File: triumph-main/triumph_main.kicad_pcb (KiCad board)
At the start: 2 copper layers, 99.1 x 86.4 mm, 81 parts, among them J1 JST_XH_vert_01x04, J10 JST_XH_vert_01x04, J2 JST_PH_vert_01x03, J3 JST_PH_vert_01x03, J4 JST_PH_vert_01x06, J5 Conn_BNC, J6 JST_PH_vert_01x03, J7 JST_PH_vert_01x06, J8 JST_PH_vert_01x03, J9 JST_PH_vert_01x03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

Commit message: Add more labels
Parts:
- moved RV1 0.13 mm to (102.9, 83.7)
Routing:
- net GND: track 98.3 -> 93.4 mm
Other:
- board text added: "1"
- board text added: "2"
- board text added: "3"
- board text added: "4"
- board text added: "COM"
- board text added: "OUTPUT GAIN ADJ"
- board text added: "PRESCALE"
- board text added: "SINE"
- board text added: "SINE ADJ"
- board text added: "TRI GEN GAIN ADJ"
- board text removed: "SIN"
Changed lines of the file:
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@@
   (general
     (thickness 1.6)
-    (drawings 61)
+    (drawings 70)
     (tracks 415)
     (zones 0)
@@
     (descr "8-lead though-hole mounted DIP package, row spacing 7.62 mm (300 mils), Socket, LongPads")
     (tags "THT DIP DIL PDIP 2.54mm 7.62mm 300mil Socket LongPads")
-    (fp_text reference U3 (at 3.81 -2.33) (layer F.SilkS)
+    (fp_text reference U3 (at 3.81 10.16) (layer F.SilkS)
       (effects (font (size 1 1) (thickness 0.15)))
     )
@@
     (descr "Potentiometer, vertical, Bourns 3296W, https://www.bourns.com/pdfs/3296.pdf")
     (tags "Potentiometer vertical Bourns 3296W")
-    (fp_text reference RV5 (at -8.89 0 180) (layer F.SilkS)
+    (fp_text reference RV5 (at 3.556 -1.27 180) (layer F.SilkS)
       (effects (font (size 1 1) (thickness 0.15)))
     )
@@
     (descr "Potentiometer, vertical, Bourns 3296W, https://www.bourns.com/pdfs/3296.pdf")
     (tags "Potentiometer vertical Bourns 3296W")
-    (fp_text reference RV4 (at -2.54 -3.66 90) (layer F.SilkS)
+    (fp_text reference RV4 (at -6.604 -4.572 180) (layer F.SilkS)
       (effects (font (size 1 1) (thickness 0.15)))
     )
@@
     (descr "Potentiometer, vertical, Bourns 3296W, https://www.bourns.com/pdfs/3296.pdf")
     (tags "Potentiometer vertical Bourns 3296W")
-    (fp_text reference RV3 (at -2.54 -3.66 90) (layer F.SilkS)
+    (fp_text reference RV3 (at -6.604 4.572) (layer F.SilkS)
       (effects (font (size 1 1) (thickness 0.15)))
     )
@@
     (descr "Potentiometer, vertical, Bourns 3296W, https://www.bourns.com/pdfs/3296.pdf")
     (tags "Potentiometer vertical Bourns 3296W")
-    (fp_text reference RV2 (at -2.54 -3.66 90) (layer F.SilkS)
+    (fp_text reference RV2 (at -6.54 4.445 180) (layer F.SilkS)
       (effects (font (size 1 1) (thickness 0.15)))
     )
@@
   )
   (module Potentiometer_THT:Potentiometer_Bourns_3296W_Vertical (layer F.Cu)
-    (at 102.87 83.82 90)
+    (at 102.87 83.693 90)
     (descr "Potentiometer, vertical, Bourns 3296W, https://www.bourns.com/pdfs/3296.pdf")
     (tags "Potentiometer vertical Bourns 3296W")
-    (fp_text reference RV1 (at -8.89 0 180) (layer F.SilkS)
+    (fp_text reference RV1 (at 3.556 1.524 180) (layer F.SilkS)
       (effects (font (size 1 1) (thickness 0.15)))
     )
@@
     )
   )
+  (gr_text PRESCALE (at 146.05 98.425) (layer F.SilkS)
+    (effects (font (size 1 1) (thickness 0.15)))
+  )
+  (gr_text "OUTPUT\nGAIN ADJ" (at 112.522 129.032) (layer F.SilkS)
+    (effects (font (size 1 1) (thickness 0.15)))
+  )
+  (gr_text "SINE ADJ" (at 138.43 79.756) (layer F.SilkS)
+    (effects (font (size 1 1) (thickness 0.15)))
+  )
+  (gr_text "TRI GEN\nGAIN ADJ" (at 102.87 93.472) (layer F.SilkS)
+    (effects (font (size 1 1) (thickness 0.15)))
+  )
+  (gr_text COM (at 127.103 63.119) (layer F.SilkS)
+    (effects (font (size 1 1) (thickness 0.15)))
+  )
+  (gr_text 4 (at 124.103 63.119) (layer F.SilkS)
+    (effects (font (size 1 1) (thickness 0.15)))
+  )
+  (gr_text 3 (at 122.103 63.119) (layer F.SilkS)
+    (effects (font (size 1 1) (thickness 0.15)))
+  )
+  (gr_text 2 (at 120.103 63.119) (layer F.SilkS)
+    (effects (font (size 1 1) (thickness 0.15)))
+  )
+  (gr_text 1 (at 118.103 63.119) (layer F.SilkS)
+    (effects (font (size 1 1) (thickness 0.15)))
+  )
   (gr_text OUT (at 103.095 110.55) (layer F.SilkS)
     (effects (font (size 1 1) (thickness 0.15)) (justify left))
@@
     (effects (font (size 1 1) (thickness 0.15)) (justify left))
   )
-  (gr_text SIN (at 103.095 102.55) (layer F.SilkS)
+  (gr_text SINE (at 103.095 102.55) (layer F.SilkS)
     (effects (font (size 1 1) (thickness 0.15)) (justify left))
   )
@@
     (effects (font (size 1.27 1.27) (thickness 0.254)))
   )
-  (gr_text "FREQ SEL" (at 122.936 63.754) (layer F.SilkS)
+  (gr_text "FREQ SEL" (at 122.936 65.024) (layer F.SilkS)
     (effects (font (size 1.27 1.27) (thickness 0.254)))
   )
@@
     (effects (font (size 1 1) (thickness 0.15)))
   )
-  (gr_line (start 158.115 113.665) (end 158.115 112.395) (layer F.SilkS) (width 0.254))
-  (gr_line (start 155.575 113.665) (end 158.115 113.665) (layer F.SilkS) (width 0.254))
-  (gr_line (start 155.575 112.395) (end 155.575 113.665) (layer F.SilkS) (width 0.254))
-  (gr_line (start 153.035 113.665) (end 153.035 112.395) (layer F.SilkS) (width 0.254))
-  (gr_line (start 153.035 112.395) (end 155.575 112.395) (layer F.SilkS) (width 0.254))
-  (gr_line (start 136.525 113.665) (end 137.795 112.395) (layer F.SilkS) (width 0.254))
-  (gr_line (start 135.255 112.395) (end 136.525 113.665) (layer F.SilkS) (width 0.254))
-  (gr_line (start 133.985 113.665) (end 135.255 112.395) (layer F.SilkS) (width 0.254))
+  (gr_line (start 156.845 113.665) (end 156.845 112.395) (layer F.SilkS) (width 0.254))
+  (gr_line (start 154.305 113.665) (end 156.845 113.665) (layer F.SilkS) (width 0.254))
+  (gr_line (start 154.305 112.395) (end 154.305 113.665) (layer F.SilkS) (width 0.254))
+  (gr_line (start 151.765 113.665) (end 151.765 112.395) (layer F.SilkS) (width 0.254))
+  (gr_line (start 151.765 112.395) (end 154.305 112.395) (layer F.SilkS) (width 0.254))
+  (gr_line (start 137.795 113.665) (end 139.065 112.395) (layer F.SilkS) (width 0.254))
+  (gr_line (start 136.525 112.395) (end 137.795 113.665) (layer F.SilkS) (width 0.254))
+  (gr_line (start 135.255 113.665) (end 136.525 112.395) (layer F.SilkS) (width 0.254))
   (gr_line (start 173.355 95.885) (end 173.355 93.345) (layer F.SilkS) (width 0.254))
   (gr_line (start 170.815 95.885) (end 173.355 95.885) (layer F.SilkS) (width 0.254))
@@
   (gr_line (start 168.275 93.345) (end 170.815 93.345) (layer F.SilkS) (width 0.254))
   (gr_line (start 168.275 95.885) (end 168.275 93.345) (layer F.SilkS) (width 0.254))
-  (gr_arc (start 141.605 94.615) (end 140.335 94.615) (angle -180) (layer F.SilkS) (width 0.254))
-  (gr_arc (start 139.065 94.615) (end 140.335 94.615) (angle -180) (layer F.SilkS) (width 0.254))
+  (gr_arc (start 142.24 94.615) (end 140.97 94.615) (angle -180) (layer F.SilkS) (width 0.254))
+  (gr_arc (start 139.7 94.615) (end 140.97 94.615) (angle -180) (layer F.SilkS) (width 0.254))
   (gr_line (start 122.555 95.885) (end 123.825 93.345) (layer F.SilkS) (width 0.254))
   (gr_line (start 121.285 93.345) (end 122.555 95.885) (layer F.SilkS) (width 0.254))
@@
   (segment (start 172.425 124.755) (end 192.405 124.755) (width 0.762) (layer B.Cu) (net 1))
   (segment (start 168.91 128.27) (end 172.425 124.755) (width 0.762) (layer B.Cu) (net 1))
-  (segment (start 138.43 88.71) (end 133.54 88.71) (width 0.762) (layer B.Cu) (net 1))
   (segment (start 141.06 60.99) (end 142.36 59.69) (width 0.762) (layer B.Cu) (net 2))
   (segment (start 141.06 63.5) (end 141.06 60.99) (width 0.762) (layer B.Cu) (net 2))
@@
   (segment (start 111.76 87.871) (end 111.76 83.82) (width 0.254) (layer F.Cu) (net 26))
   (segment (start 111.76 88.9) (end 111.76 87.871) (width 0.254) (layer F.Cu) (net 26))
-  (segment (start 105.32 91.35) (end 102.87 88.9) (width 0.254) (layer F.Cu) (net 27))
+  (segment (start 102.87 88.9) (end 102.87 88.773) (width 0.254) (layer F.Cu) (net 27))
   (segment (start 111.76 91.35) (end 105.32 91.35) (width 0.254) (layer F.Cu) (net 27))
+  (segment (start 105.32 91.35) (end 102.87 88.9) (width 0.254) (layer F.Cu) (net 27))
   (segment (start 170.27 73.66) (end 170.27 77.47) (width 0.254) (layer F.Cu) (net 28))
   (segment (start 168.04 85.09) (end 168.91 85.09) (width 0.254) (layer F.Cu) (net 28))
@@
   (segment (start 150.495 123.19) (end 150.495 121.101) (width 0.254) (layer F.Cu) (net 35))
   (segment (start 150.495 121.101) (end 150.044 120.65) (width 0.254) (layer F.Cu) (net 35))
-  (segment (start 102.87 86.36) (end 102.87 83.82) (width 0.254) (layer F.Cu) (net 38))
   (segment (start 121.92 107.95) (end 120.65 107.95) (width 0.254) (layer F.Cu) (net 38))
   (segment (start 120.65 107.95) (end 120.015 107.315) (width 0.254) (layer F.Cu) (net 38))
@@
   (segment (start 114.175 70.755) (end 112.76 70.755) (width 0.254) (layer F.Cu) (net 38))
   (segment (start 112.76 70.755) (end 112.395 71.12) (width 0.254) (layer F.Cu) (net 38))
-  (segment (start 102.87 80.645) (end 102.87 83.82) (width 0.254) (layer B.Cu) (net 38))
-  (segment (start 112.395 71.12) (end 102.87 80.645) (width 0.254) (layer B.Cu) (net 38))
   (segment (start 125.73 70.755) (end 128.54 70.755) (width 0.254) (layer F.Cu) (net 38))
   (segment (start 128.54 70.755) (end 129.54 71.755) (width 0.254) (layer F.Cu) (net 38))
   (segment (start 129.54 71.755) (end 129.54 83.82) (width 0.254) (layer F.Cu) (net 38))
   (segment (start 129.54 83.82) (end 128.27 85.09) (width 0.254) (layer F.Cu) (net 38))
+  (segment (start 102.87 86.233) (end 102.87 83.693) (width 0.254) (layer F.Cu) (net 38))
+  (segment (start 102.87 80.645) (end 102.87 83.693) (width 0.254) (layer B.Cu) (net 38))
+  (segment (start 112.395 71.12) (end 102.87 80.645) (width 0.254) (layer B.Cu) (net 38))
   (segment (start 121.92 68.305) (end 121.92 65.405) (width 0.254) (layer F.Cu) (net 39))
   (segment (start 122.11 65.215) (end 122.11 59.055) (width 0.254) (layer F.Cu) (net 39))
@@
     (connect_pads (clearance 0.508))
     (min_thickness 0.254)
-    (fill yes (arc_segments 32) (thermal_gap 0.508) (thermal_bridge_width 0.508))
+    (fill (arc_segments 32) (thermal_gap 0.508) (thermal_bridge_width 0.508))
     (polygon
       (pts

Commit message: Finish routing
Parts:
- added G***: LOGO, triumph-logos:cit-ee-l, B.Cu at (144.1, 136.5)
- added G***: LOGO, triumph-logos:ruddock-crest-l, B.Cu at (177.8, 111.1)
- moved G*** 2.44 mm to (183.5, 103.5)

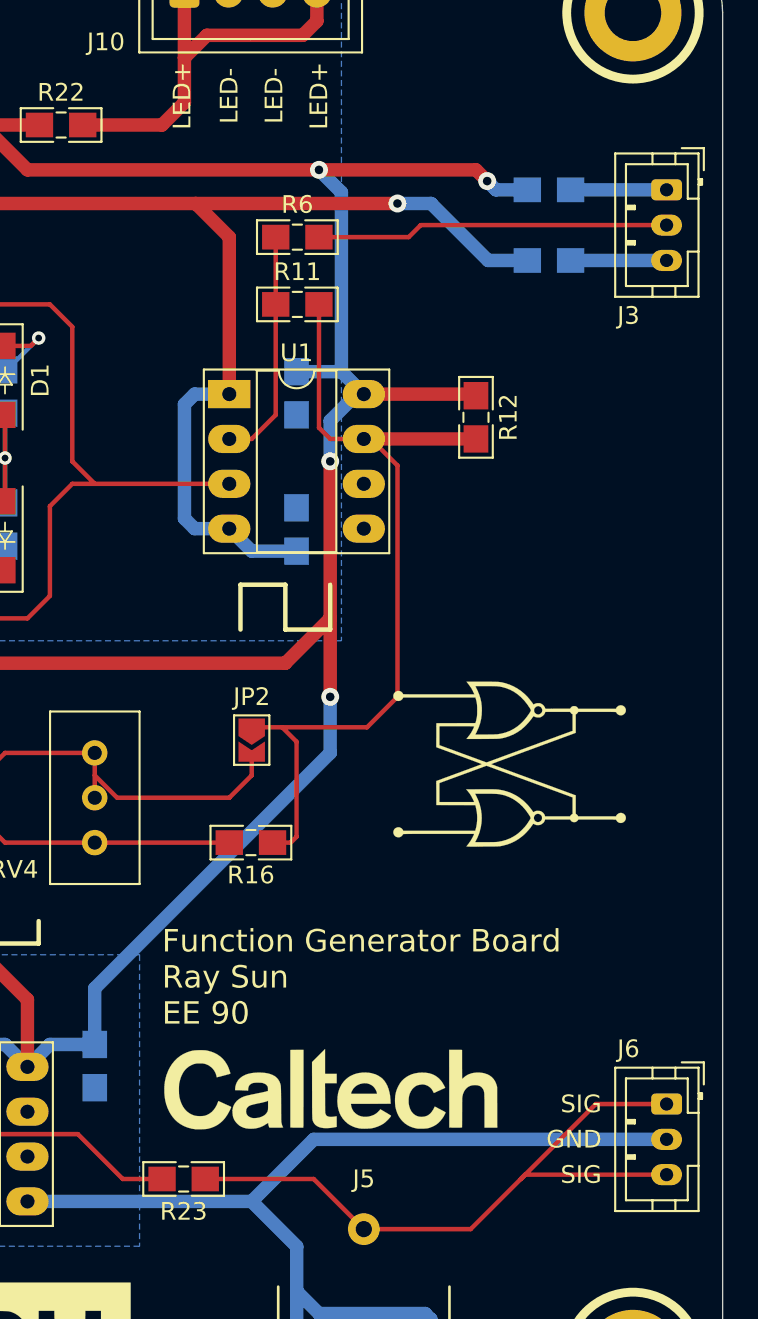
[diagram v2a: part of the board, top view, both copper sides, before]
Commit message: Add missing conector labels
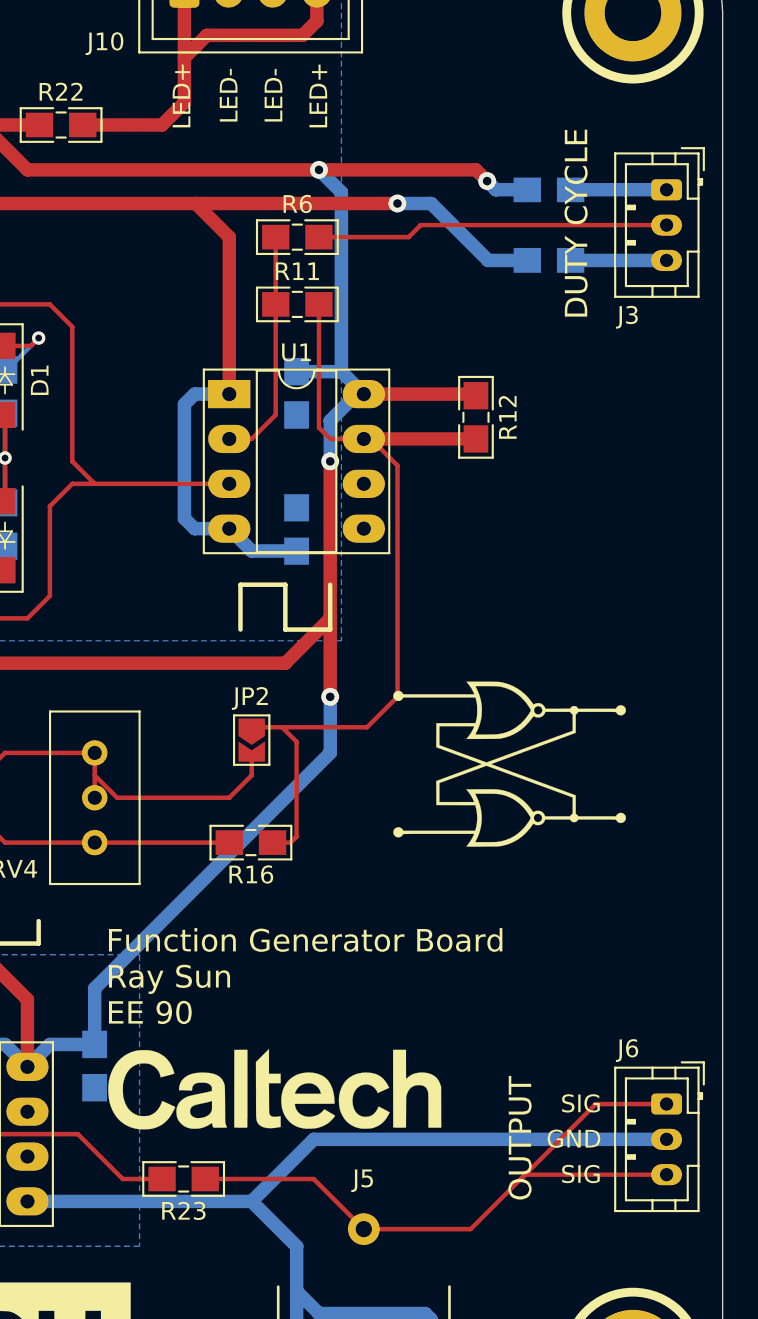
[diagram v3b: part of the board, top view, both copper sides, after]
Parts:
- moved G*** 3.17 mm to (170.2, 121.9)
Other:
- board text added: "DUTY CYCLE"
- board text added: "OUTPUT"
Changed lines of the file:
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@@
   (general
     (thickness 1.6)
-    (drawings 70)
+    (drawings 72)
     (tracks 415)
     (zones 0)
@@
   )
   (module triumph-logos:caltech (layer F.Cu)
-    (at 173.355 121.92)
+    (at 170.18 121.92)
     (fp_text reference G*** (at 0 0) (layer F.SilkS) hide
       (effects (font (size 1.524 1.524) (thickness 0.3)))
@@
     )
   )
+  (gr_text OUTPUT (at 184.15 124.714 90) (layer F.SilkS)
+    (effects (font (size 1.27 1.27) (thickness 0.254)))
+  )
+  (gr_text "DUTY CYCLE" (at 187.325 72.898 90) (layer F.SilkS)
+    (effects (font (size 1.27 1.27) (thickness 0.254)))
+  )
   (gr_text PRESCALE (at 146.05 98.425) (layer F.SilkS)
     (effects (font (size 1 1) (thickness 0.15)))
@@
     (arrow2b (pts (xy 175.26 148.589999) (xy 176.386504 148.003578)))
   )
-  (gr_text "Function Generator Board\nRay Sun\nEE 90" (at 163.83 115.57) (layer F.SilkS)
+  (gr_text "Function Generator Board\nRay Sun\nEE 90" (at 160.655 115.57) (layer F.SilkS)
     (effects (font (size 1.27 1.27) (thickness 0.2032)) (justify left))
   )

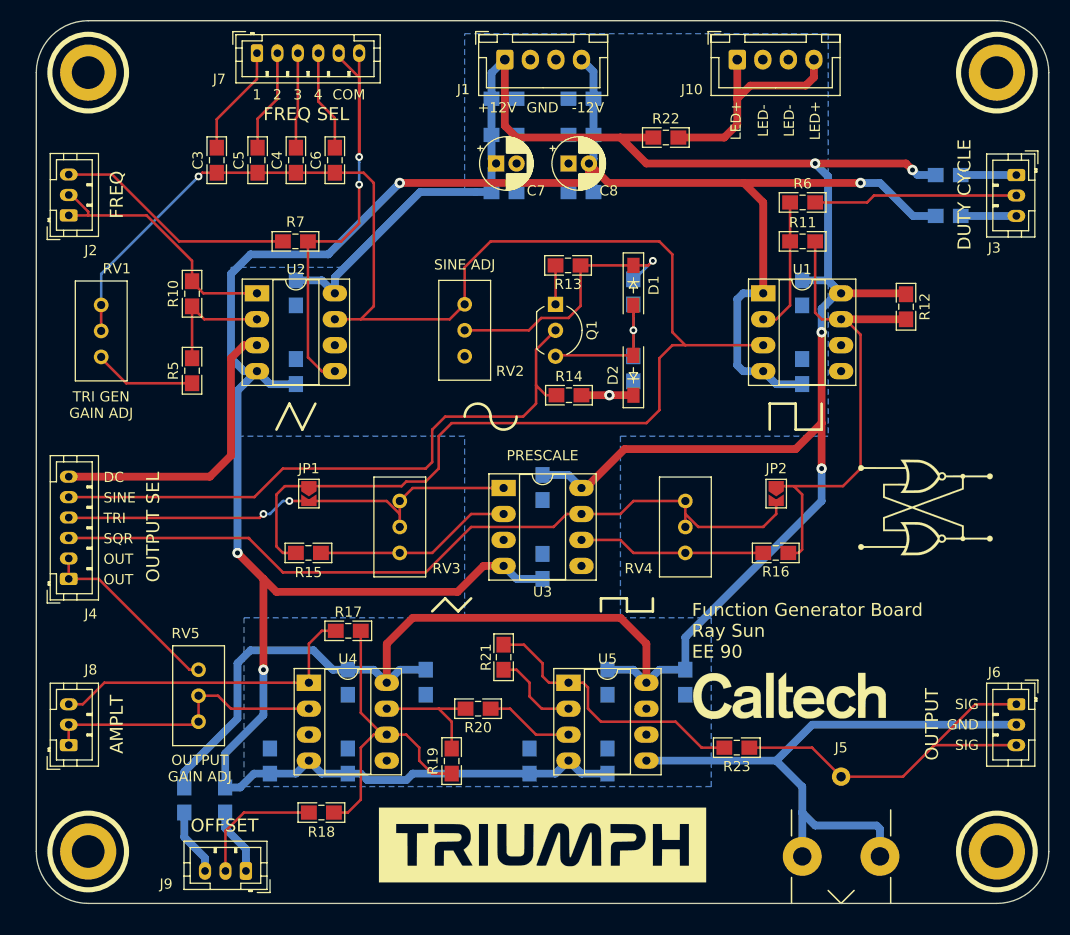
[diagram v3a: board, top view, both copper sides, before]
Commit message: Make some traces thicker, 50 mil power
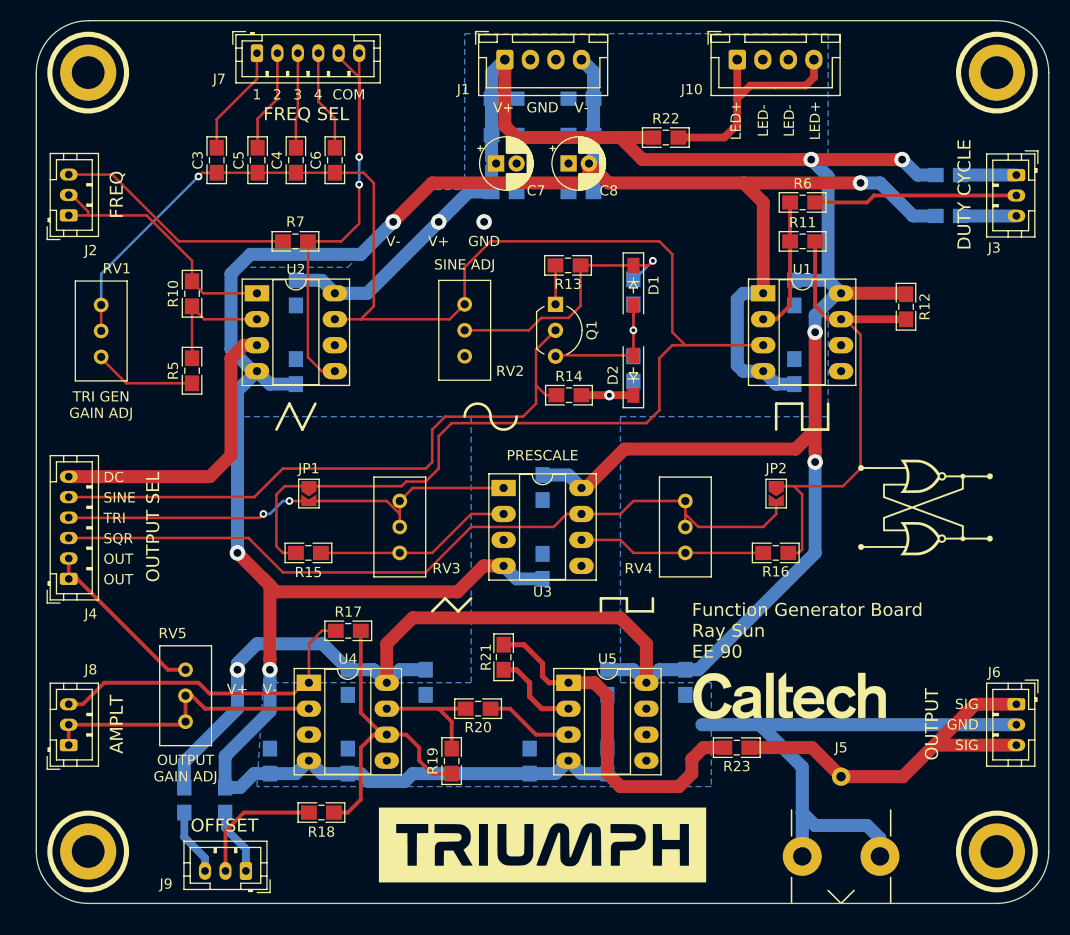
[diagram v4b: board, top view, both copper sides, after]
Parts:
- moved RV5 1.27 mm to (111.1, 119.4)
- moved C1 0.76 mm to (170.7, 82.5)
- moved C2 0.76 mm to (170.7, 90.2)
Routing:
- net Net-(R21-Pad1): track 27.7 -> 35.0 mm
- net GND: track 93.4 -> 90.2 mm, vias 1 -> 2
- net /SIG_PREOUT: track 18.4 -> 17.1 mm
- net /APL_2: track 31.3 -> 32.2 mm
- net -12V: track 247.7 -> 247.1 mm
- net +12V: track 268.4 -> 269.0 mm, vias 4 -> 6
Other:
- board text added: "V+"
- board text added: "V-"
- board text removed: "+12V"
- board text removed: "-12V"

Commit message: Make thicker intermediate signal traces, more labels
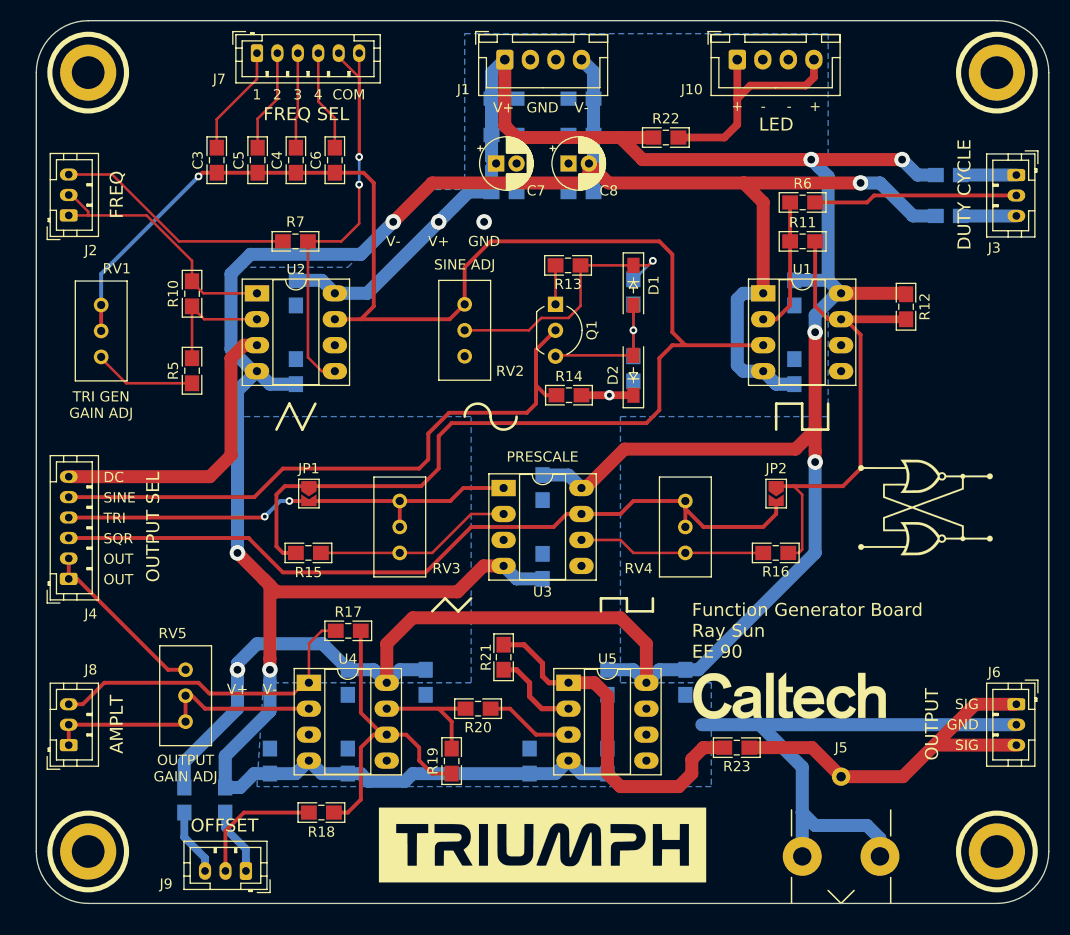
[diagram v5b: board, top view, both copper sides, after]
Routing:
- net /SIG_TRI: track 46.8 -> 46.3 mm
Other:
- board text added: "+"
- board text added: "-"
- board text added: "LED"
- board text removed: "LED+"
- board text removed: "LED-"
